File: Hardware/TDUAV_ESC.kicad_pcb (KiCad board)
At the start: 2 copper layers, 100 x 70 mm, 74 parts, among them J1 USB_B_Micro, J2 PWM-UBEC, J3 UART, J4 CH340, J5 BATT, J6 GND, J7 PHASE_A, J8 PHASE_B, J9 PHASE_C, Q1 IRLZ44NS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

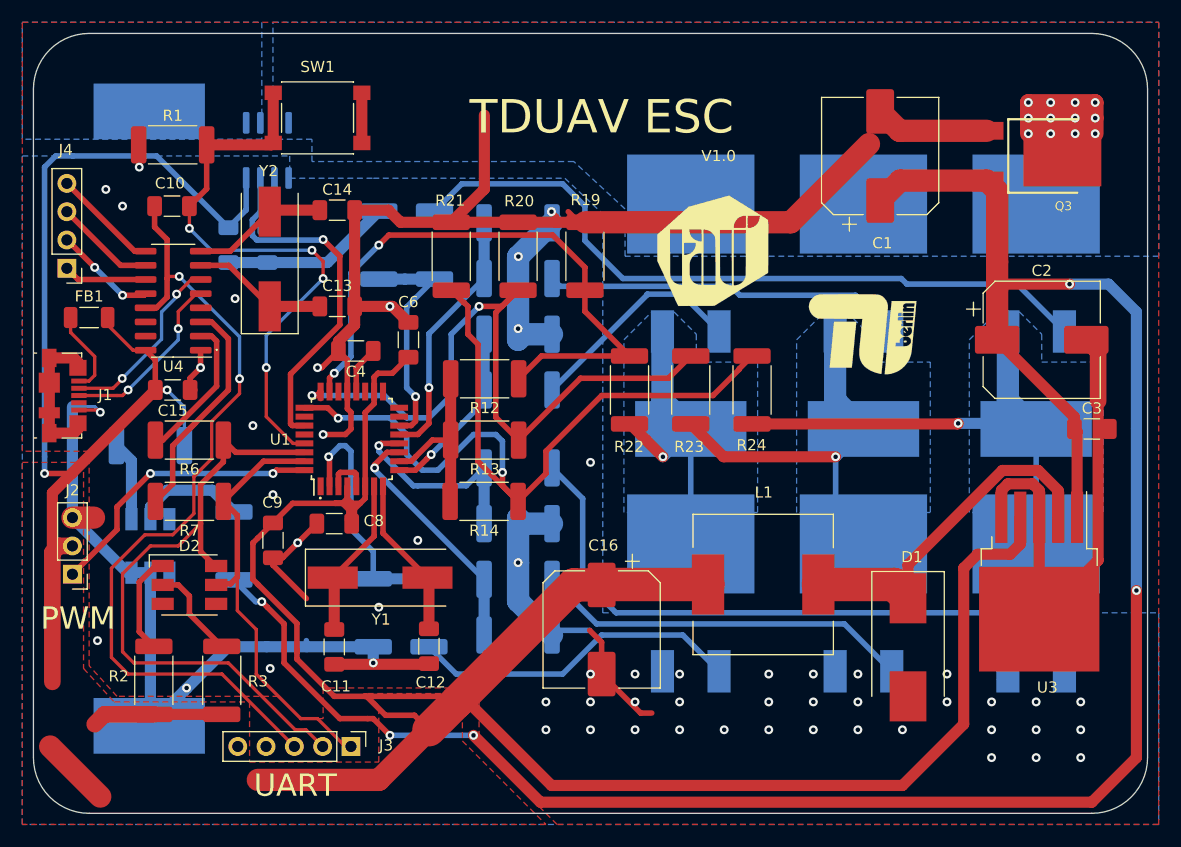
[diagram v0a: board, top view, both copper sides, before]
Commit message: Edited Silkscreens
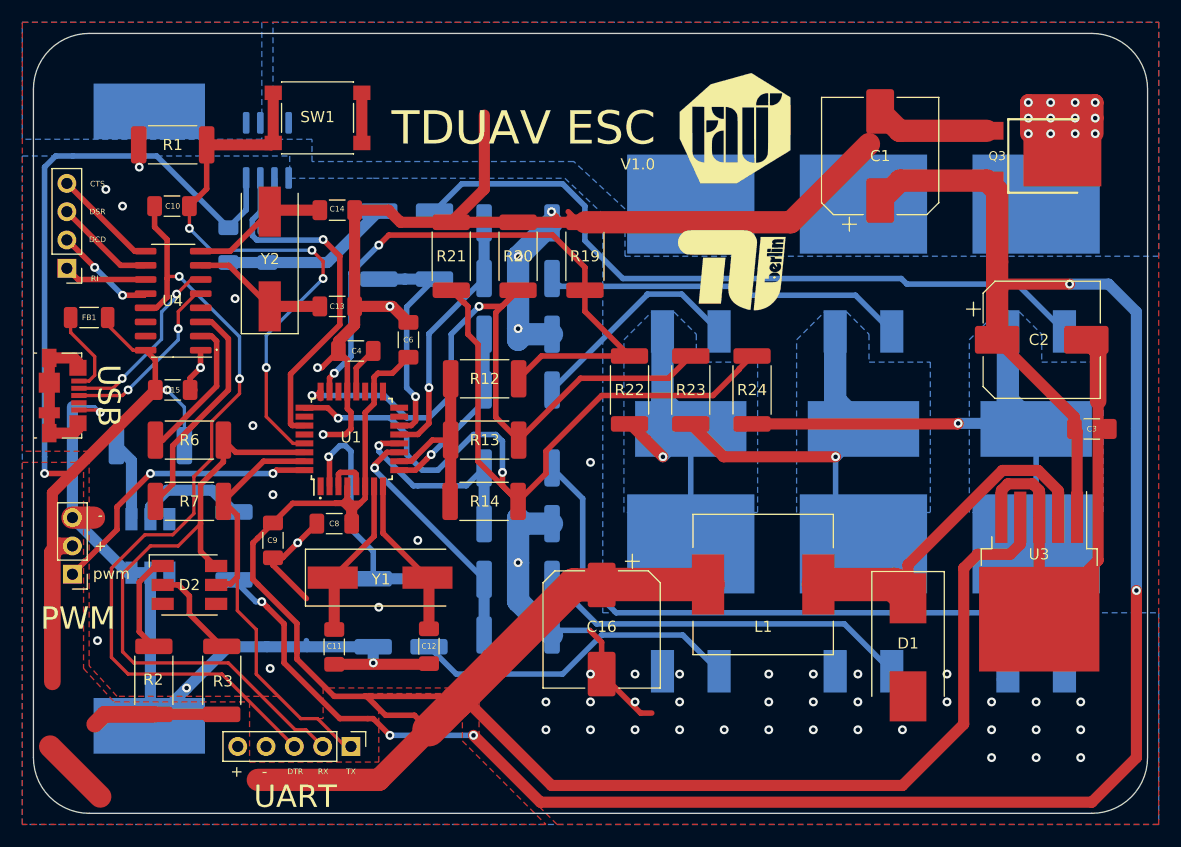
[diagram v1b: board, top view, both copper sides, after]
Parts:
- moved G*** 13.1 mm to (162.8, 71.2)
- moved G*** 11.2 mm to (163.0, 58.5)
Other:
- board text added: "+"
- board text added: "-"
- board text added: "CTS"
- board text added: "DCD"
- board text added: "DSR"
- board text added: "DTR"
- board text added: "RI"
- board text added: "RX"
- board text added: "TX"
- board text added: "USB"
- board text added: "pwm"

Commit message: Added cap to ch340 and changed values of decoupling caps
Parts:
- removed G***: LOGO, LOGO:TUB
- removed G***: LOGO, LOGO:TDU
- added C17: 100nF, Capacitor_SMD:C_1206_3216Metric_Pad1.33x1.80mm_HandSolder, F.Cu at (120.3, 81.3)
- C15: value 10nF -> 100nF
- moved C5 1.00 mm to (122.0, 69.0)
- turned R7 to 0 degrees
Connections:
- D2 pad 3: Net-(D2-Pad3) -> (no net)
- D2 pad 4: Net-(D2-Pad4) -> (no net)
- D3 pad 3: Net-(D3-Pad3) -> (no net)
- D3 pad 4: Net-(D3-Pad4) -> (no net)
- J1 pad 4: Net-(J1-Pad4) -> (no net)
- R7 pad 1: TX -> Net-(R7-Pad1)
- R7 pad 2: Net-(R7-Pad2) -> TX
- U1 pad 1: Net-(U1-Pad1) -> (no net)
- U1 pad 15: Net-(U1-Pad15) -> (no net)
- U1 pad 16: Net-(U1-Pad16) -> (no net)
- U1 pad 17: Net-(U1-Pad17) -> (no net)
- U1 pad 19: Net-(U1-Pad19) -> (no net)
- U1 pad 22: Net-(U1-Pad22) -> (no net)
- U1 pad 26: Net-(U1-Pad26) -> (no net)
- U1 pad 28: Net-(U1-Pad28) -> (no net)
- U4 pad 14: Net-(U4-Pad14) -> (no net)
- U4 pad 15: Net-(U4-Pad15) -> (no net)
- U4 pad 3: Net-(R7-Pad2) -> Net-(R7-Pad1)
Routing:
- net GND: track 320.5 -> 452.9 mm
- net VCC: track 319.2 -> 342.8 mm
- net Net-(R7-Pad2): track 21.1 -> 0.00 mm
- net Net-(R7-Pad1): track 0.00 -> 20.4 mm
- net Net-(C17-Pad2): track 0.00 -> 8.00 mm
- net RESET: track 52.4 -> 44.5 mm, vias 4 -> 2
- net BEMF_A: track 55.5 -> 53.5 mm
- net AMP_SENS: track 32.3 -> 31.1 mm
- net DTR: track 74.5 -> 73.8 mm

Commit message: Updated PCB design
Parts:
- added G***: LOGO, LOGO:TUB, F.Cu at (163.2, 71.2)
- added G***: LOGO, LOGO:TDU, F.Cu at (163.2, 58.4)
- moved J4 1.14 mm to (103.5, 72.1)
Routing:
- net DCD: track 9.18 -> 8.14 mm
- net DSR: track 9.06 -> 8.14 mm
- net RI: track 7.49 -> 6.57 mm
- net GND: track 452.9 -> 453.5 mm, vias 55 -> 56
